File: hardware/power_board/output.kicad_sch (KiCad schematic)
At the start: 19 parts, among them J6 HEATER-L, J8 HEATER-E, J9 HEATER-N, K1 HEATER-TOP, K2 HEATER-BOTTOM, Q1 MMBT3904, Q2 MMBT3904, U6 PC817, U7 PC817

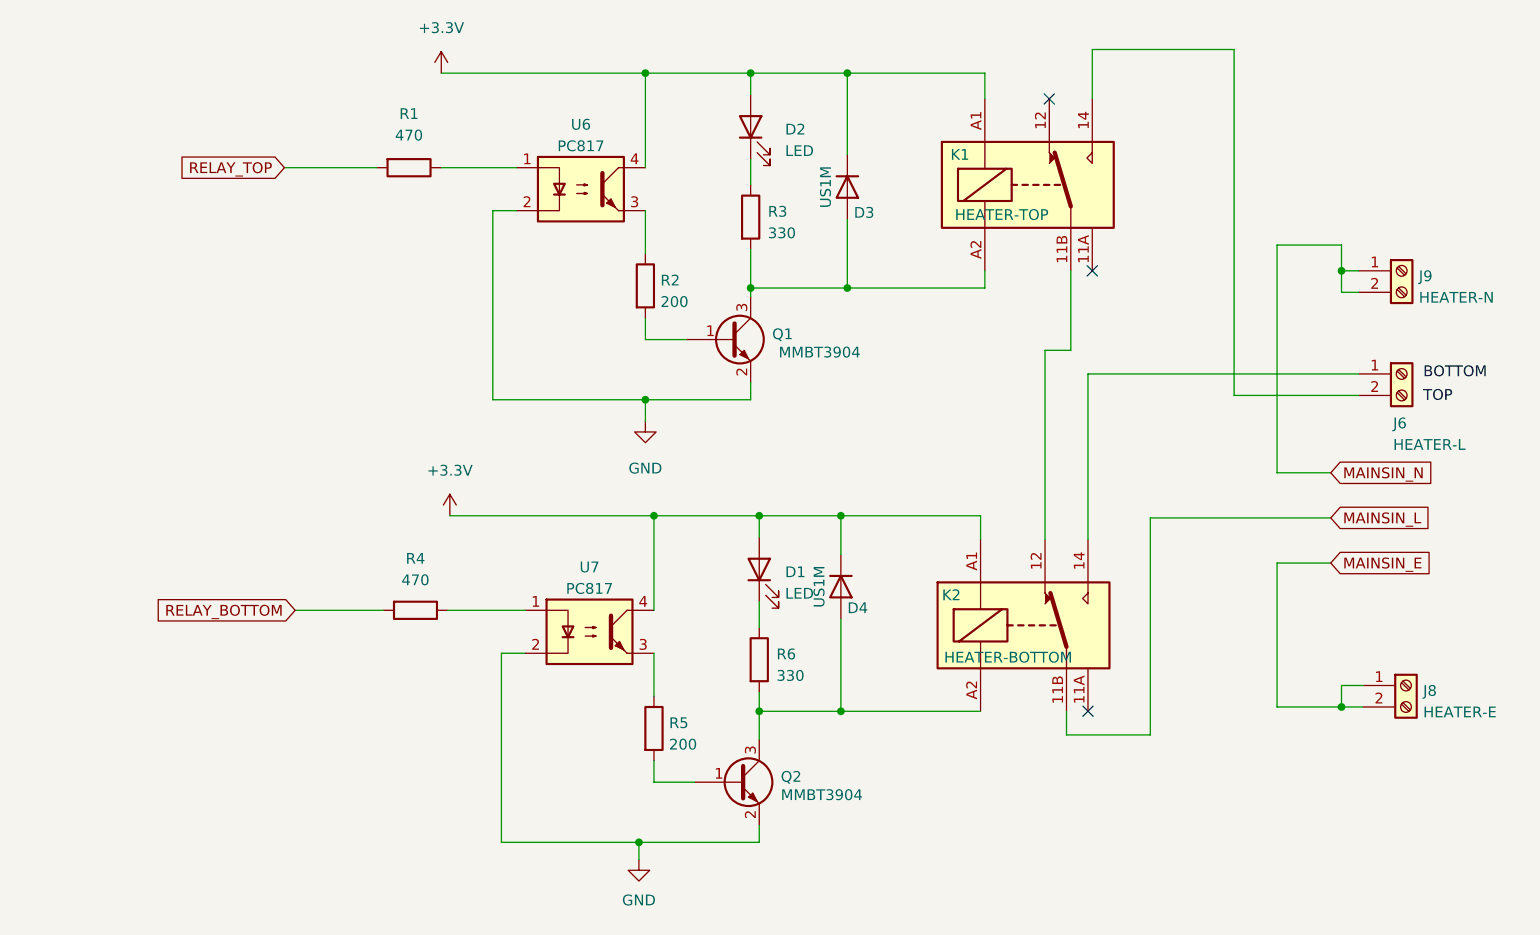
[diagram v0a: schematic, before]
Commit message: v2 Power/Relay PCB
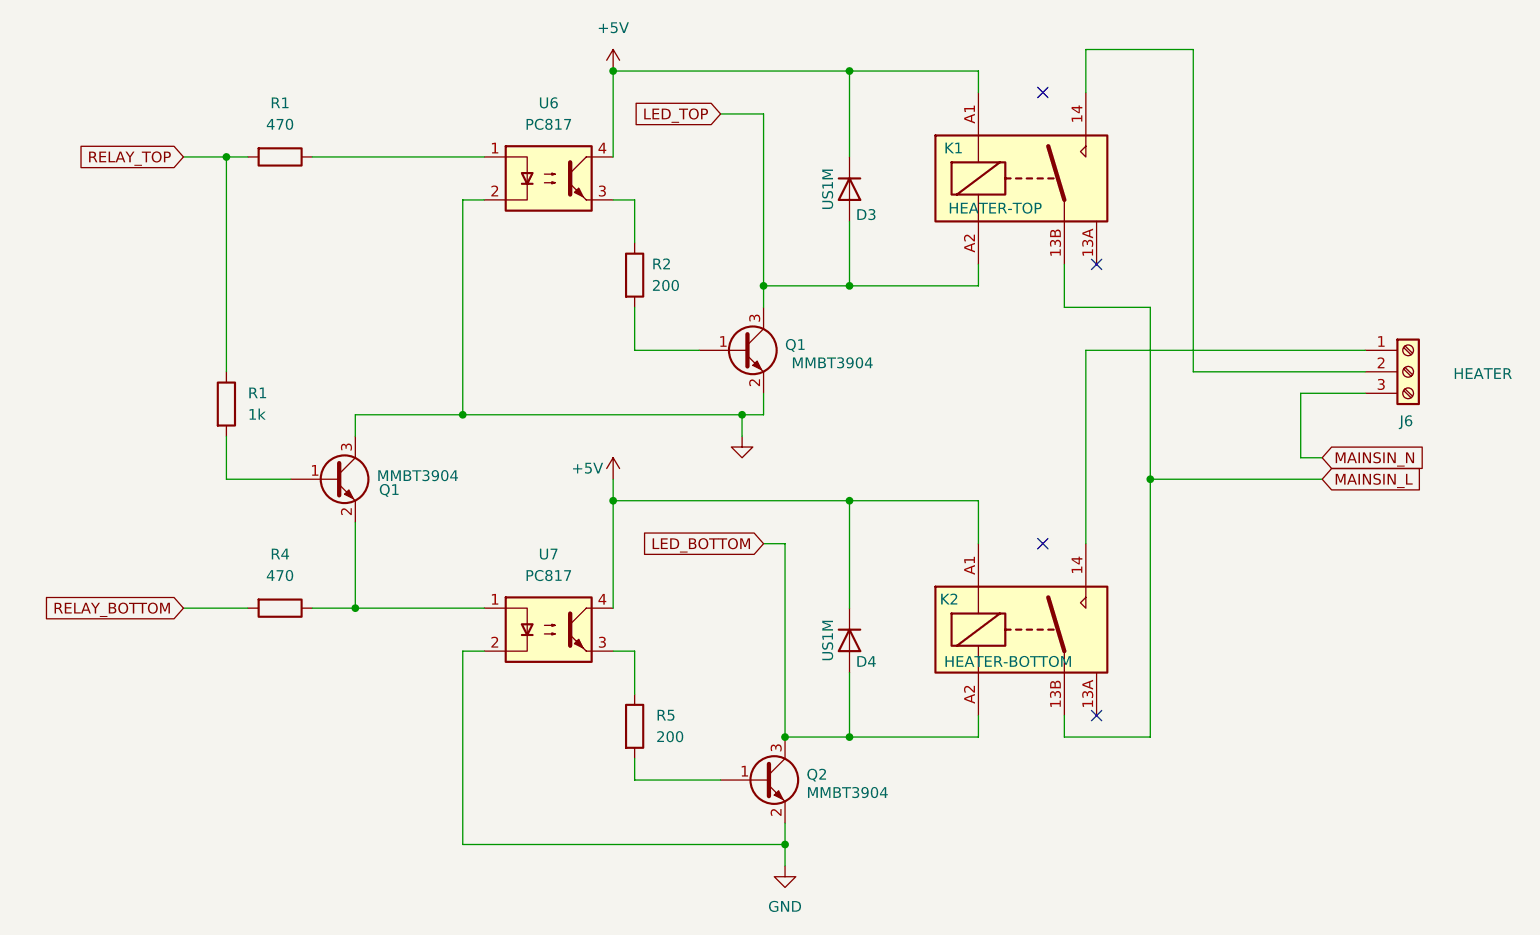
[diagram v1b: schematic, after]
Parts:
- removed D1, D2: LED, LED_THT:LED_D5.0mm_Clear, symbol Device:LED
- removed J8: HEATER-E, TerminalBlock_Dinkle:TerminalBlock_Dinkle_DT-55-B01X-02_P10.00mm, symbol Connector:Screw_Terminal_01x02
- removed J9: HEATER-N, TerminalBlock_Dinkle:TerminalBlock_Dinkle_DT-55-B01X-02_P10.00mm, symbol Connector:Screw_Terminal_01x02
- removed R3, R6: 330, Resistor_SMD:R_0805_2012Metric, symbol Device:R
- added Q1: MMBT3904, Package_TO_SOT_SMD:SOT-23, symbol Transistor_BJT:MMBT3904
- added R1: 1k, Resistor_SMD:R_0805_2012Metric, symbol Device:R
- J6: value HEATER-L -> HEATER; footprint TerminalBlock_Dinkle:TerminalBlock_Dinkle_DT-55-B01X-02_P10.00mm -> TerminalBlock_Dinkle:TerminalBlock_Dinkle_DT-55-B01X-03_P10.00mm; symbol Connector:Screw_Terminal_01x02 -> Connector:Screw_Terminal_01x03
- K1, K2: footprint Relay_THT:Relay_SPDT_RAYEX-L90 -> Relay_THT:Relay_SPST_RAYEX-L90A; symbol Relay:RAYEX-L90 -> Relay:RAYEX-L90A
- U6, U7: footprint Package_DIP:DIP-4_W7.62mm -> Package_DIP:DIP-4_W7.62mm_SMDSocket_SmallPads
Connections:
- net GND: now also Q1.3 (C)
- net MAINSIN_L: now also K1.13B, K2.13B; no longer K2.11B
- net MAINSIN_N: now also J6.3 (Pin_3)
- net RELAY_TOP: now also R1.1
- net LED_TOP: now reaches D3.2 (A), K1.A2, Q1.3 (C)
- net at R4.1, U7.1: now also Q1.2 (E)
- net LED_BOTTOM: now reaches D4.2 (A), K2.A2, Q2.3 (C)
- net +3.3V renamed +5V
- new net: Q1.1 (B), R1.2
- no-connect marks 3 -> 4
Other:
- moved on the sheet: D4, Q1, Q2, R1, R2, R4, R5, U6, U7

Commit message: Refactored PCBs for v2. See README
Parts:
- J6: footprint TerminalBlock_Dinkle:TerminalBlock_Dinkle_DT-55-B01X-03_P10.00mm -> TerminalBlock2:HB9500-9.5-3P
- U6, U7: footprint Package_DIP:DIP-4_W7.62mm_SMDSocket_SmallPads -> PC817XI:SOIC254P975X460-4N
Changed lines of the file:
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@@
       (effects (font (size 1.27 1.27)))
     )
-    (property "Footprint" "Package_DIP:DIP-4_W7.62mm_SMDSocket_SmallPads" (at 99.06 60.96 0)
+    (property "Footprint" "PC817XI:SOIC254P975X460-4N" (at 99.06 60.96 0)
       (effects (font (size 1.27 1.27) italic) (justify left) hide)
     )
@@
       (effects (font (size 1.27 1.27)) (justify left))
     )
-    (property "Footprint" "TerminalBlock_Dinkle:TerminalBlock_Dinkle_DT-55-B01X-03_P10.00mm" (at 205.74 78.74 0)
+    (property "Footprint" "TerminalBlock2:HB9500-9.5-3P" (at 205.74 78.74 0)
       (effects (font (size 1.27 1.27)) hide)
     )
@@
       (effects (font (size 1.27 1.27)))
     )
-    (property "Footprint" "Package_DIP:DIP-4_W7.62mm_SMDSocket_SmallPads" (at 99.06 114.3 0)
+    (property "Footprint" "PC817XI:SOIC254P975X460-4N" (at 99.06 114.3 0)
       (effects (font (size 1.27 1.27) italic) (justify left) hide)
     )

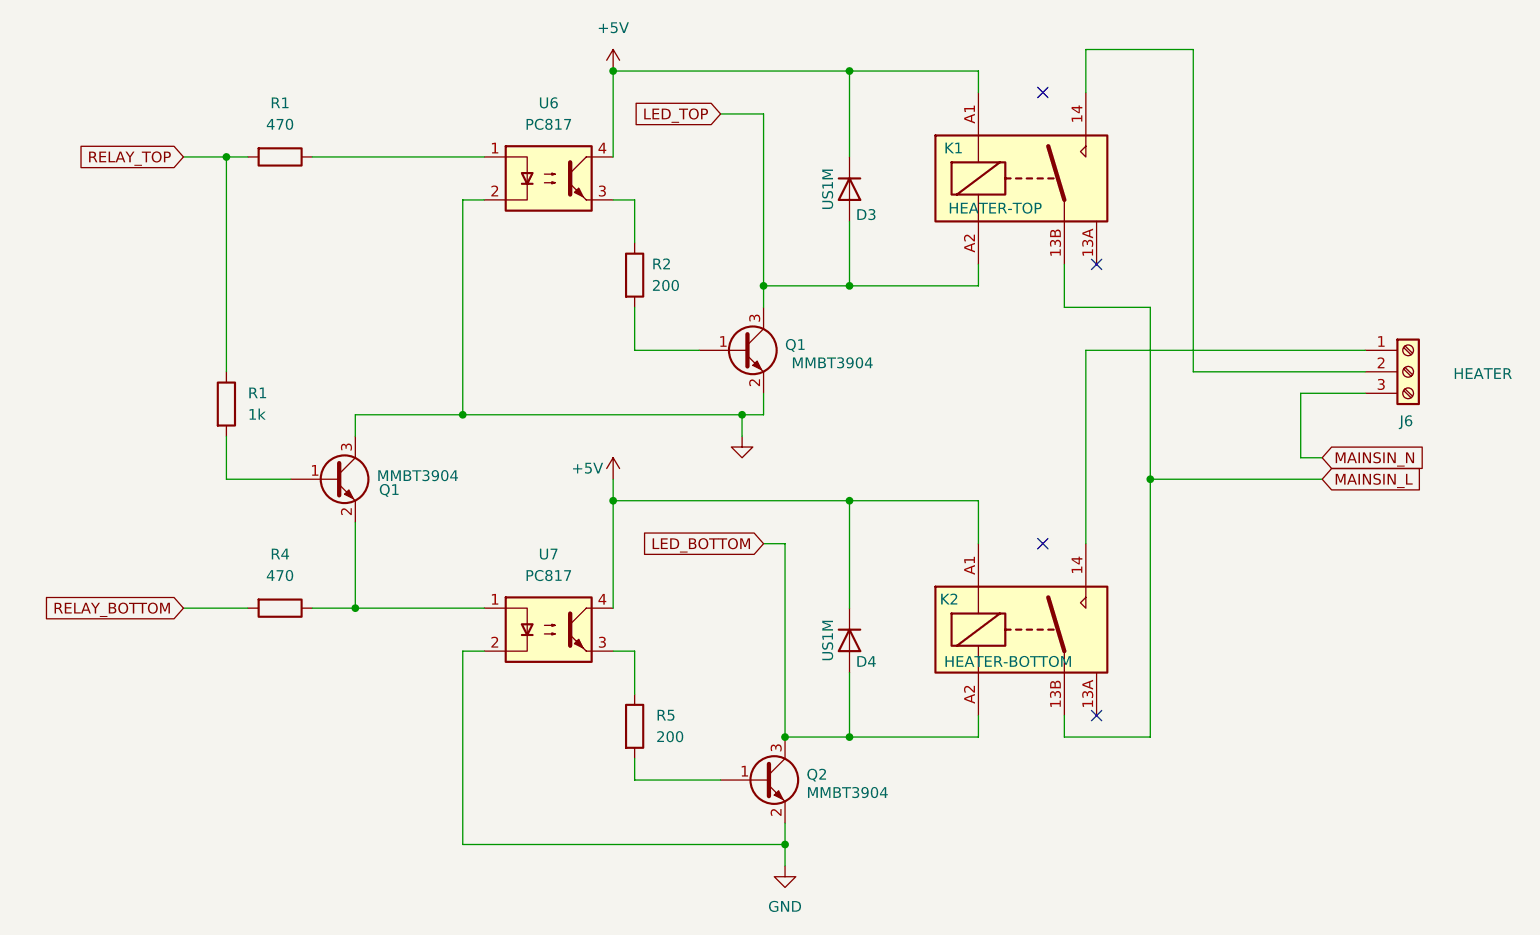
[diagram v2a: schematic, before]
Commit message: fix boards so they components are on the correct side lol
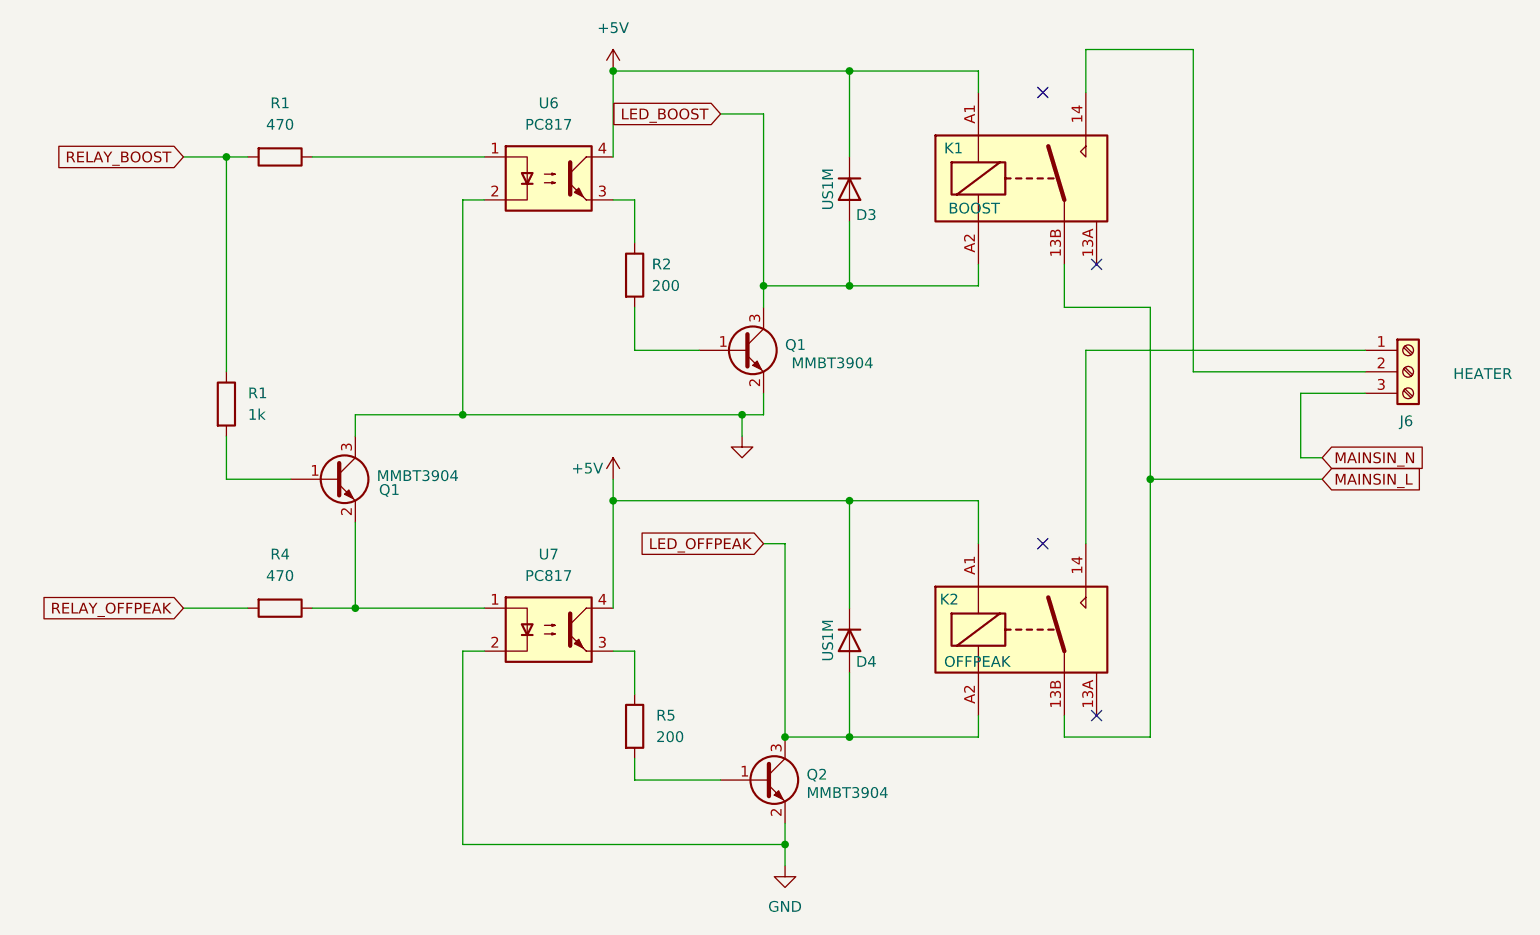
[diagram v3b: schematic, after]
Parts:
- K1: value HEATER-TOP -> BOOST
- K2: value HEATER-BOTTOM -> OFFPEAK
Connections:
- net LED_BOTTOM renamed LED_OFFPEAK
- net LED_TOP renamed LED_BOOST
- net RELAY_BOTTOM renamed RELAY_OFFPEAK
- net RELAY_TOP renamed RELAY_BOOST
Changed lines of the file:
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@@
     (stroke (width 0) (type default))
   )
-  (global_label "RELAY_TOP" (shape input) (at 60.96 53.34 180) (fields_autoplaced)
+  (global_label "RELAY_BOOST" (shape input) (at 60.96 53.34 180) (fields_autoplaced)
     (effects (font (size 1.27 1.27)) (justify right))
-    (property "Intersheetrefs" "${INTERSHEET_REFS}" (at 47.8942 53.34 0)
+    (property "Intersheetrefs" "${INTERSHEET_REFS}" (at 45.2748 53.34 0)
       (effects (font (size 1.27 1.27)) (justify right) hide)
     )
   )
-  (global_label "LED_BOTTOM" (shape input) (at 129.54 99.06 180) (fields_autoplaced)
+  (global_label "LED_OFFPEAK" (shape input) (at 129.54 99.06 180) (fields_autoplaced)
     (effects (font (size 1.27 1.27)) (justify right))
-    (property "Intersheetrefs" "${INTERSHEET_REFS}" (at 114.8225 99.06 0)
+    (property "Intersheetrefs" "${INTERSHEET_REFS}" (at 113.8548 99.06 0)
       (effects (font (size 1.27 1.27)) (justify right) hide)
     )
   )
-  (global_label "LED_TOP" (shape input) (at 124.46 48.26 180) (fields_autoplaced)
+  (global_label "LED_BOOST" (shape input) (at 124.46 48.26 180) (fields_autoplaced)
     (effects (font (size 1.27 1.27)) (justify right))
-    (property "Intersheetrefs" "${INTERSHEET_REFS}" (at 113.492 48.26 0)
+    (property "Intersheetrefs" "${INTERSHEET_REFS}" (at 110.952 48.26 0)
       (effects (font (size 1.27 1.27)) (justify right) hide)
     )
   )
-  (global_label "RELAY_BOTTOM" (shape input) (at 60.96 106.68 180) (fields_autoplaced)
+  (global_label "RELAY_OFFPEAK" (shape input) (at 60.96 106.68 180) (fields_autoplaced)
     (effects (font (size 1.27 1.27)) (justify right))
-    (property "Intersheetrefs" "${INTERSHEET_REFS}" (at 44.1447 106.68 0)
+    (property "Intersheetrefs" "${INTERSHEET_REFS}" (at 43.0976 106.68 0)
       (effects (font (size 1.27 1.27)) (justify right) hide)
     )
@@
       (effects (font (size 1.27 1.27)) (justify left))
     )
-    (property "Value" "HEATER-TOP" (at 151.384 59.436 0)
+    (property "Value" "BOOST" (at 151.384 59.436 0)
       (effects (font (size 1.27 1.27)) (justify left))
     )
@@
       (effects (font (size 1.27 1.27)) (justify left))
     )
-    (property "Value" "HEATER-BOTTOM" (at 150.876 113.03 0)
-      (effects (font (size 1.27 1.27)) (justify left))
-    )
+    (property "Value" "OFFPEAK" (at 150.876 113.03 0)
+      (effects (font (size 1.27 1.27)) (justify left))
+    )

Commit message: v3 first draft
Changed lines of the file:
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@@
     (stroke (width 0) (type default))
   )
-  (wire (pts (xy 129.54 48.26) (xy 129.54 68.58))
+  (wire (pts (xy 129.54 48.006) (xy 129.54 68.58))
     (stroke (width 0) (type default))
   )
@@
     (stroke (width 0) (type default))
   )
-  (wire (pts (xy 124.46 48.26) (xy 129.54 48.26))
+  (wire (pts (xy 125.476 48.006) (xy 129.54 48.006))
     (stroke (width 0) (type default))
   )
@@
     )
   )
-  (global_label "LED_BOOST" (shape input) (at 124.46 48.26 180) (fields_autoplaced)
+  (global_label "LED_BOOST" (shape input) (at 125.476 48.006 180) (fields_autoplaced)
     (effects (font (size 1.27 1.27)) (justify right))
-    (property "Intersheetrefs" "${INTERSHEET_REFS}" (at 110.952 48.26 0)
+    (property "Intersheetrefs" "${INTERSHEET_REFS}" (at 111.968 48.006 0)
       (effects (font (size 1.27 1.27)) (justify right) hide)
     )
